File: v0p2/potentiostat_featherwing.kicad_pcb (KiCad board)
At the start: 2 copper layers, 22.9 x 50.8 mm, 20 parts, among them J1 Screw_Terminal_01x03, J2 Conn_01x03, J3 Conn_01x02, U1 feather_wing, U2 ADG702, U3 MCP6004

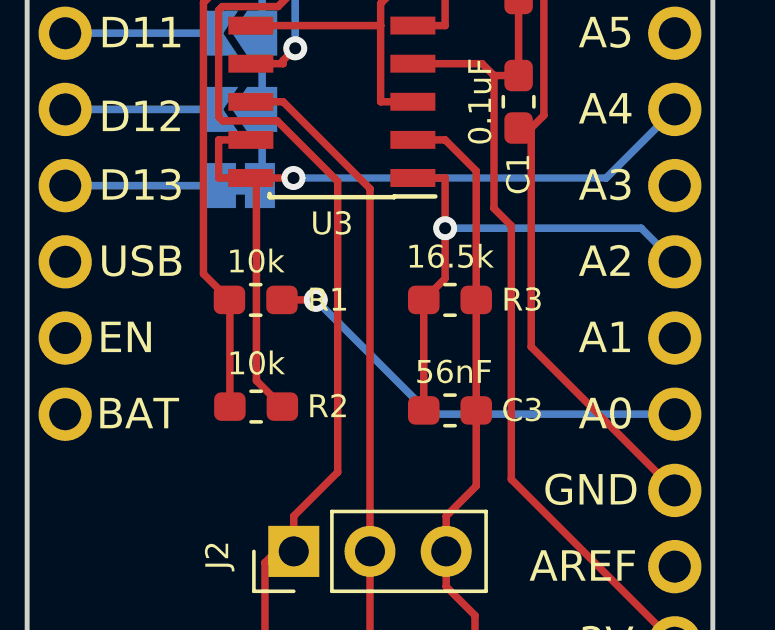
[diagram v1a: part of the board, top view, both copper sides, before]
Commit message: Minor modifications for schematic - no substantive changes. Remade gerber files for v0p2_r2.
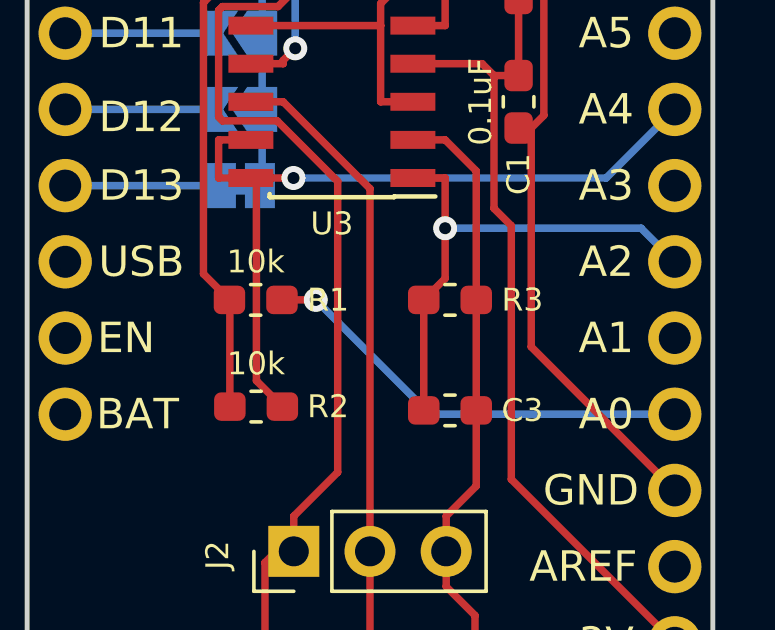
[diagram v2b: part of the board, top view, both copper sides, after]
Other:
- board text added: "Rodeostat Featherwing v0.2 www.iorodeo.com"
- board text removed: "Potentiostat Featherwing v0.1 www.iorodeo.com"
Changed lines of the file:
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@@
       (effects (font (size 0.762 0.762) (thickness 0.1524)))
     )
-    (fp_text value 56nF (at -0.127 1.27 180) (layer F.SilkS)
+    (fp_text value 56nF (at -0.127 1.27 180) (layer F.SilkS) hide
       (effects (font (size 0.762 0.762) (thickness 0.1524)))
     )
@@
       (effects (font (size 0.762 0.762) (thickness 0.1524)))
     )
-    (fp_text value 16.5k (at 0 1.43 180) (layer F.SilkS)
+    (fp_text value 16.5k (at 0 1.43 180) (layer F.SilkS) hide
       (effects (font (size 0.762 0.762) (thickness 0.1524)))
     )
@@
   (gr_arc (start 41.91 73.66) (end 39.37 73.66) (angle -90) (layer Edge.Cuts) (width 0.15))
   (gr_arc (start 41.91 27.94) (end 41.91 25.4) (angle -90) (layer Edge.Cuts) (width 0.15))
-  (gr_text "Potentiostat Featherwing v0.1\nwww.iorodeo.com" (at 51.435 44.45 90) (layer B.SilkS)
+  (gr_text "Rodeostat Featherwing v0.2\nwww.iorodeo.com" (at 51.435 44.45 90) (layer B.SilkS)
     (effects (font (size 1.016 1.016) (thickness 0.2032)) (justify mirror))
   )
